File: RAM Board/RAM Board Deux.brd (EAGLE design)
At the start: 148.8 x 100 mm, 25 parts, among them IC1 74LS32N, IC2 74LS04N, IC3 74LS138N, IC4 74LS32N, IC6 74LS32N, U1 AS6C4008, U2 AS6C4008, U3 AS6C4008, U4 AS6C4008, U5 AS6C4008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

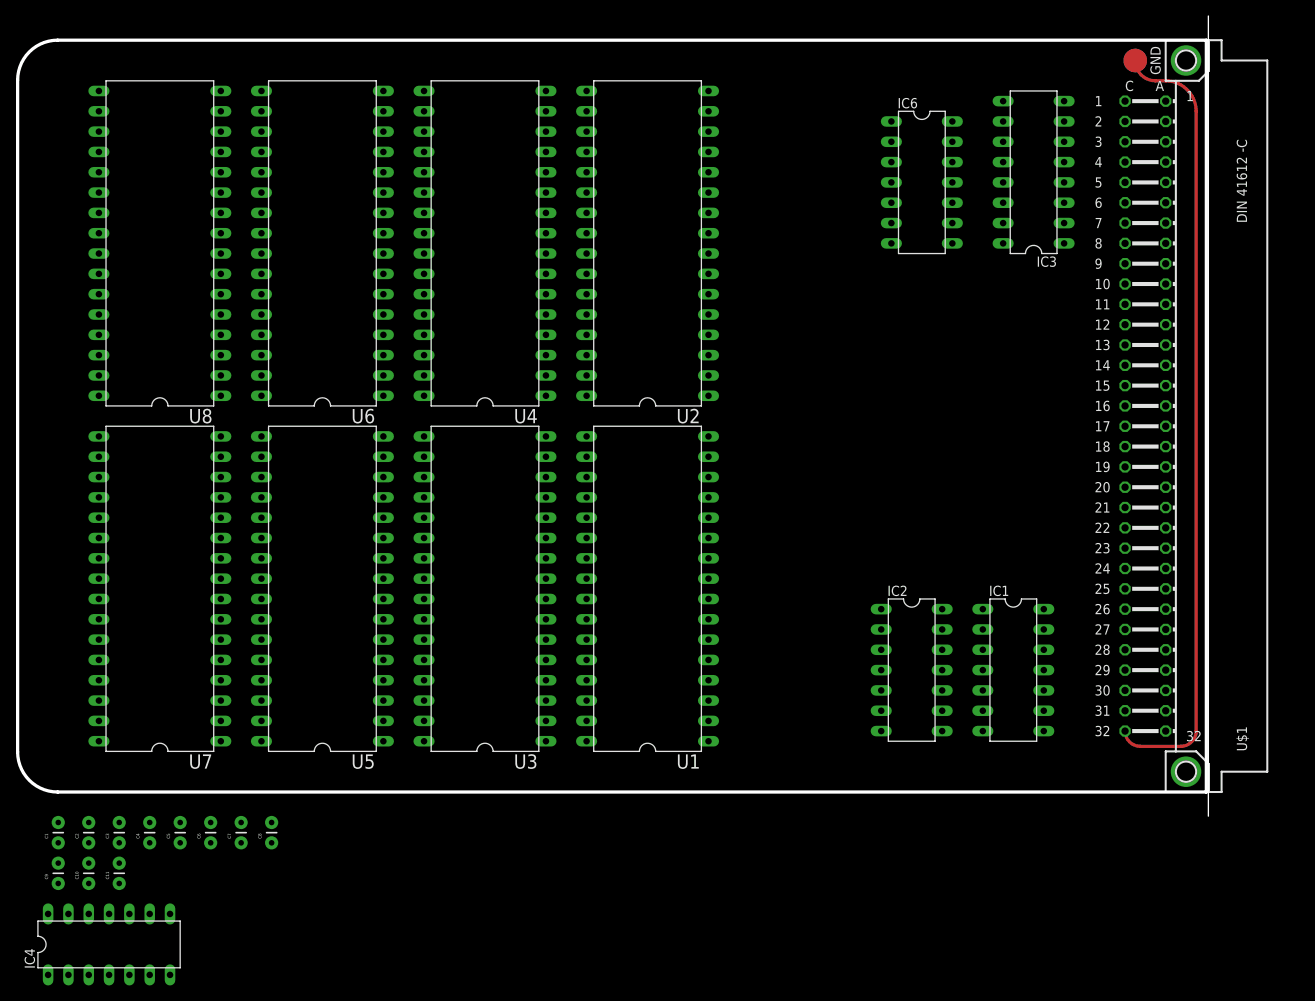
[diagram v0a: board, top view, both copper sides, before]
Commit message: Built breakout board and RAM card
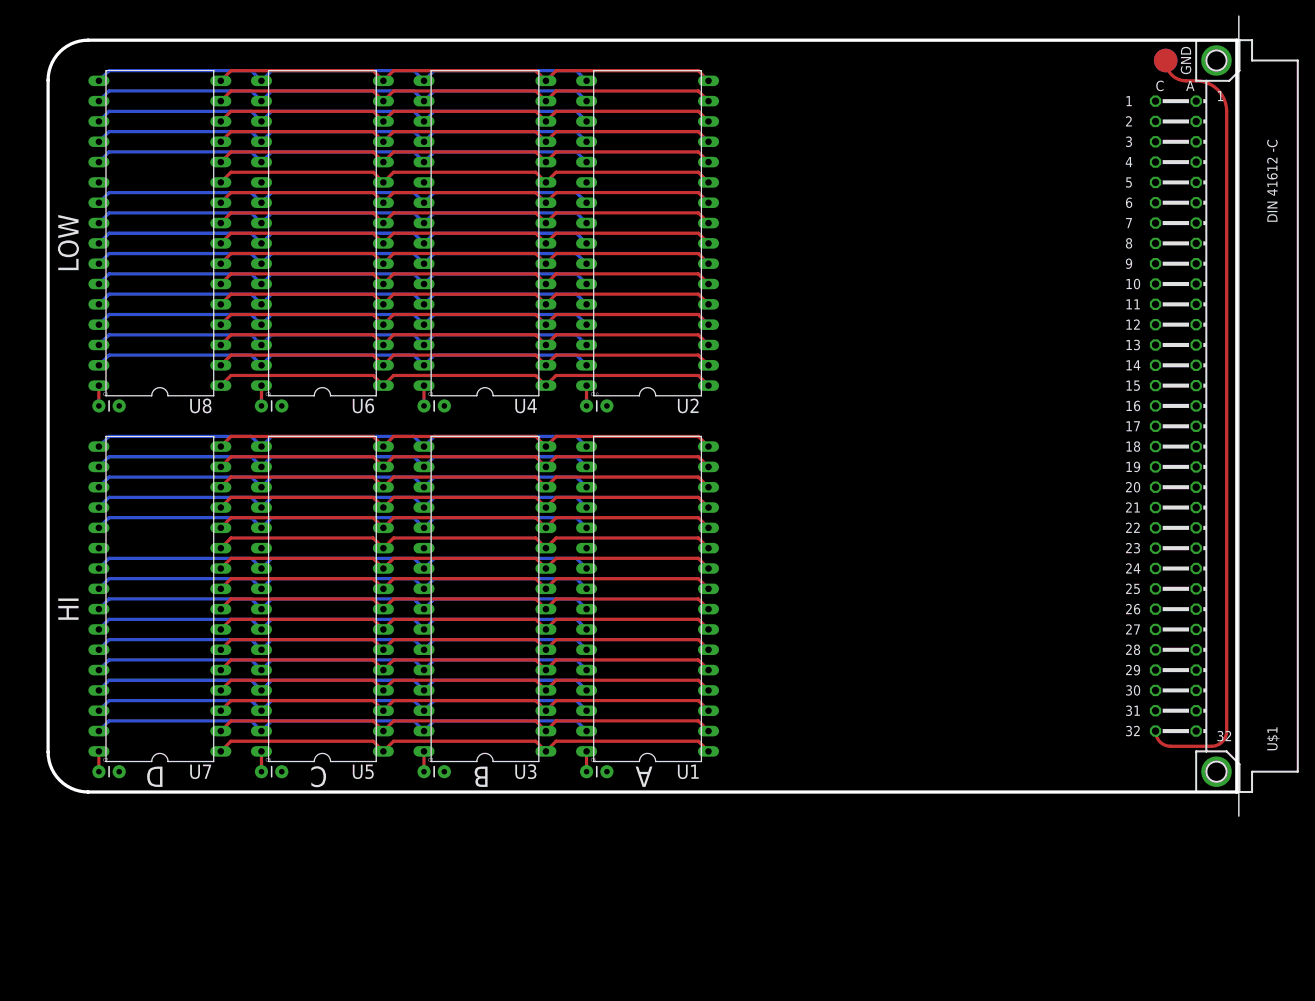
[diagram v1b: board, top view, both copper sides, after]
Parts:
- removed C11, C4, C5: 100nF, SparkFun-Capacitors:CAP-PTH-SMALL
- removed IC1, IC4, IC6: 74LS32N, 74xx-us:DIL14
- removed IC2: 74LS04N, 74xx-eu:DIL14
- removed IC3: 74LS138N, 74xx-eu:DIL16
- moved C10 86.2 mm to (67.3, 52.1), turned to 0 degrees
- moved C3 66.6 mm to (47.0, 52.1), turned to 0 degrees
- moved C9 64.9 mm to (26.7, 52.1), turned to 0 degrees
- moved C1 54.8 mm to (6.35, 52.1), turned to 0 degrees
- moved C6 47.8 mm to (67.3, 6.35), turned to 0 degrees
- moved C7 24.5 mm to (47.0, 6.35), turned to 0 degrees
- moved C2 8.98 mm to (6.35, 6.35), turned to 0 degrees
- moved C8 8.98 mm to (26.7, 6.35), turned to 0 degrees
- moved U$1 3.81 mm to (67.3, 50.8)
- moved U1 1.27 mm to (74.9, 26.7)
- moved U3 1.27 mm to (54.6, 26.7)
- moved U5 1.27 mm to (34.3, 26.7)
- moved U7 1.27 mm to (14.0, 26.7)
- moved U2 1.27 mm to (74.9, 72.4)
- moved U4 1.27 mm to (54.6, 72.4)
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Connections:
- removed net /BOOT: IC6.1, IC6.12, IC6.4, IC6.9
- removed net /DTACK: IC2.12
- removed net N$1: IC4.10, IC4.3
- removed net N$18: IC3.9, IC6.2
- removed net N$2: IC4.6, IC4.9
- removed net N$20: IC3.11, IC6.10
- removed net N$22: IC3.13, IC6.13
- removed net N$24: IC3.15, IC6.5
- removed net N$3: IC1.2, IC1.5, IC2.2
- removed net N$4: IC2.13, IC4.8
- new net ADDRESS19: U$1.A0
- new net ADDRESS22: U$1.A18
- new net ADDRESS23: U$1.A17
- new net ADDRESS24: U$1.A16
- new net ADDRESS25: U$1.A15
- new net ADDRESS26: U$1.A14
- new net ADDRESS27: U$1.A13
- new net ADDRESS28: U$1.A12
- new net ADDRESS29: U$1.A11
- new net ADDRESS30: U$1.A10
- new net ADDRESS31: U$1.A9
- new net ADDRESS32: U$1.A8
- new net ADDRESS33: U$1.A7
- new net ADDRESS34: U$1.A6
- new net ADDRESS35: U$1.A5
- new net ADDRESS36: U$1.A4
- new net ADDRESS37: U$1.A3
- new net ADDRESS38: U$1.A20
- new net ADDRESS39: U$1.A21
- new net DATA16: U$1.D0
- new net DATA17: U$1.D1
- new net DATA18: U$1.D2
- new net DATA19: U$1.D3
- new net DATA20: U$1.D4
- new net DATA21: U$1.D5
- new net DATA22: U$1.D6
- new net DATA23: U$1.D7
- new net DATA24: U$1.D8
- new net DATA25: U$1.D9
- new net DATA26: U$1.D10
- new net DATA27: U$1.D11
- new net DATA28: U$1.D12
- new net DATA29: U$1.D13
- new net DATA30: U$1.D14
- new net DATA31: U$1.D15
- new net GND1: U$1.GND
- new net S$1: C2.1, U7.32
- new net VCC1: U$1.5V
- net /AS: no longer IC3.1
- net /LDS: no longer IC1.12, IC1.4
- net /UDS: no longer IC1.1, IC1.9
- net ADDRESS0: no longer U$1.A0
- net ADDRESS1: no longer U$1.A1
- net ADDRESS10: no longer U$1.A10
- net ADDRESS11: no longer U$1.A11
- net ADDRESS12: no longer U$1.A12
- net ADDRESS13: no longer U$1.A13
- net ADDRESS14: no longer U$1.A14
- net ADDRESS15: no longer U$1.A15
- net ADDRESS16: no longer U$1.A16
- net ADDRESS17: no longer U$1.A17
- net ADDRESS18: no longer U$1.A18
- net ADDRESS2: no longer U$1.A2
- net ADDRESS20: now also U$1.A1; no longer IC3.2, U$1.A20
- net ADDRESS21: now also U$1.A2; no longer IC3.3, U$1.A21
- net ADDRESS3: no longer U$1.A3
- net ADDRESS4: no longer U$1.A4
- net ADDRESS5: no longer U$1.A5
- net ADDRESS6: no longer U$1.A6
- net ADDRESS7: no longer U$1.A7
- net ADDRESS8: no longer U$1.A8
- net ADDRESS9: no longer U$1.A9
- net BANKACS: no longer IC4.4, IC6.6
- net BANKBCS: no longer IC4.5, IC6.11
- net BANKCCS: no longer IC4.1, IC6.8
- net BANKDCS: no longer IC4.2, IC6.3
- net DATA0: no longer U$1.D0
- net DATA1: no longer U$1.D1
- net DATA10: no longer U$1.D10
- net DATA11: no longer U$1.D11
- net DATA12: no longer U$1.D12
- net DATA13: no longer U$1.D13
- net DATA14: no longer U$1.D14
- net DATA15: no longer U$1.D15
- net DATA2: no longer U$1.D2
- net DATA3: no longer U$1.D3
- net DATA4: no longer U$1.D4
- net DATA5: no longer U$1.D5
- net DATA6: no longer U$1.D6
- net DATA7: no longer U$1.D7
- net DATA8: no longer U$1.D8
- net DATA9: no longer U$1.D9
- net GND: no longer C11.2, C4.2, C5.2, IC1.7, IC2.7, IC3.4, IC3.5, IC3.8, IC4.7, IC6.7, U$1.GND
- net R/W: no longer IC1.10, IC1.13, IC2.1
- net READHI: no longer IC1.3
- net READLO: no longer IC1.6
- net VCC: no longer C11.1, C2.1, C4.1, C5.1, IC1.14, IC2.14, IC3.16, IC3.6, IC4.14, IC6.14, U$1.5V, U7.32
- net WRITEHI: no longer IC1.8
- net WRITELO: no longer IC1.11
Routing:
- net ADDRESS9: track 0.00 -> 128.2 mm
- net ADDRESS13: track 0.00 -> 128.2 mm
- net GND: track 0.00 -> 128.2 mm
- net ADDRESS7: track 0.00 -> 128.2 mm
- net ADDRESS5: track 0.00 -> 128.2 mm
- net ADDRESS18: track 0.00 -> 128.2 mm
- net ADDRESS17: track 0.00 -> 128.2 mm
- net ADDRESS16: track 0.00 -> 128.2 mm
- net ADDRESS15: track 0.00 -> 128.2 mm
- net ADDRESS14: track 0.00 -> 128.2 mm
- net ADDRESS12: track 0.00 -> 128.2 mm
- net ADDRESS10: track 0.00 -> 128.2 mm
- net ADDRESS8: track 0.00 -> 128.2 mm
- net ADDRESS2: track 0.00 -> 128.2 mm
- net ADDRESS11: track 0.00 -> 128.2 mm
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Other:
- board text added: "A"
- board text added: "B"
- board text added: "C"
- board text added: "D"
- board text added: "HI"
- board text added: "LOW"
